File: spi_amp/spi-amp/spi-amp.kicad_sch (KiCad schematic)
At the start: 35 parts, among them J1 IN+, J2 IN-, J3 OUT+, J4 OUT-, J5 Conn_01x02, J7 Conn_01x06, U1 LMH6401, U2 LM78M05_TO220, U3 LTV-847S, U4 74LVC1G04, U5 74LVC1G04, U6 74LVC1G04

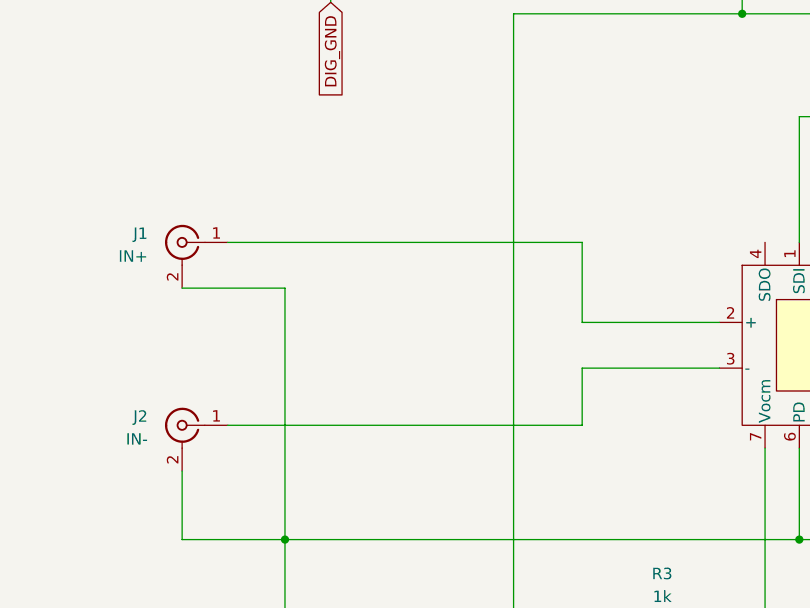
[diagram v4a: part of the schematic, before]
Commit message: Added input capacitors.
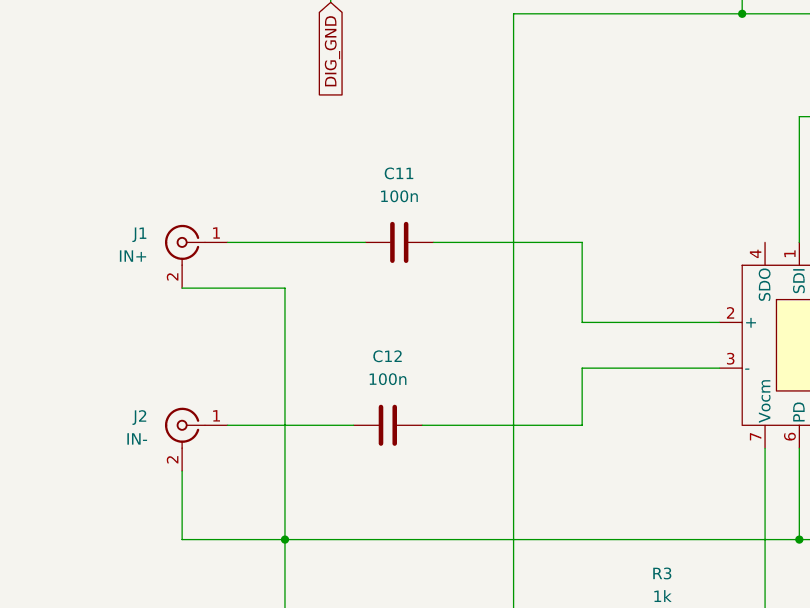
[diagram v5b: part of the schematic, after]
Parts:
- added C11, C12: 100n, Capacitor_SMD:C_0805_2012Metric_Pad1.18x1.45mm_HandSolder, symbol Device:C
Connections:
- net at J2.1 (In): now also C12.1; no longer U1.3 (-)
- net at J1.1 (In): now also C11.1; no longer U1.2 (+)
- new net: C11.2, U1.2 (+)
- new net: C12.2, U1.3 (-)
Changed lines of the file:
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@@
-	(wire
-		(pts
-			(xy 52.07 81.28) (xy 91.44 81.28)
-		)
-		(stroke
-			(width 0)
-			(type default)
-		)
-	)
 	(wire
 		(pts
@@
 	(wire
 		(pts
+			(xy 52.07 81.28) (xy 67.31 81.28)
+		)
+		(stroke
+			(width 0)
+			(type default)
+		)
+	)
+	(wire
+		(pts
 			(xy 119.38 81.28) (xy 119.38 71.12)
 		)
@@
 	(wire
 		(pts
+			(xy 73.66 101.6) (xy 91.44 101.6)
+		)
+		(stroke
+			(width 0)
+			(type default)
+		)
+	)
+	(wire
+		(pts
 			(xy 83.82 124.46) (xy 96.52 124.46)
 		)
@@
 	(wire
 		(pts
+			(xy 91.44 81.28) (xy 74.93 81.28)
+		)
+		(stroke
+			(width 0)
+			(type default)
+		)
+	)
+	(wire
+		(pts
 			(xy 224.79 34.29) (xy 224.79 142.24)
 		)
@@
 	(wire
 		(pts
-			(xy 52.07 101.6) (xy 91.44 101.6)
-		)
-		(stroke
-			(width 0)
-			(type default)
-		)
-	)
-	(wire
-		(pts
 			(xy 153.67 46.99) (xy 170.18 46.99)
 		)
@@
 		(pts
 			(xy 54.61 34.29) (xy 63.5 34.29)
+		)
+		(stroke
+			(width 0)
+			(type default)
+		)
+	)
+	(wire
+		(pts
+			(xy 52.07 101.6) (xy 66.04 101.6)
 		)
 		(stroke
@@
 	(symbol
 		(lib_id "Device:C")
+		(at 71.12 81.28 90)
+		(unit 1)
+		(body_style 1)
+		(exclude_from_sim no)
+		(in_bom yes)
+		(on_board yes)
+		(in_pos_files yes)
+		(dnp no)
+		(fields_autoplaced yes)
+		(property "Reference" "C11"
+			(at 71.12 73.66 90)
+			(show_name no)
+			(do_not_autoplace no)
+			(effects
+				(font
+					(size 1.27 1.27)
+				)
+			)
+		)
+		(property "Value" "100n"
+			(at 71.12 76.2 90)
+			(show_name no)
+			(do_not_autoplace no)
+			(effects
+				(font
+					(size 1.27 1.27)
+				)
+			)
+		)
+		(property "Footprint" "Capacitor_SMD:C_0805_2012Metric_Pad1.18x1.45mm_HandSolder"
+			(at 74.93 80.3148 0)
+			(hide yes)
+			(show_name no)
+			(do_not_autoplace no)
+			(effects
+				(font
+					(size 1.27 1.27)
+				)
+			)
+		)
+		(property "Datasheet" ""
+			(at 71.12 81.28 0)
+			(hide yes)
+			(show_name no)
+			(do_not_autoplace no)
+			(effects
+				(font
+					(size 1.27 1.27)
+				)
+			)
+		)
+		(property "Description" "Unpolarized capacitor"
+			(at 71.12 81.28 0)
+			(hide yes)
+			(show_name no)
+			(do_not_autoplace no)
+			(effects
+				(font
+					(size 1.27 1.27)
+				)
+			)
+		)
+		(pin "1"
+		)
+		(pin "2"
+		)
+		(instances
+			(project "spi-amp"
+				(path "/7b23121c-57e3-4266-95bd-22be68c11a42"
+					(reference "C11")
+					(unit 1)
+				)
+			)
+		)
+	)
+	(symbol
+		(lib_id "Device:C")
 		(at 252.73 151.13 180)
 		(unit 1)
@@
 					(unit 1)
 				)
+			)
+		)
+	)
+	(symbol
+		(lib_id "Device:C")
+		(at 69.85 101.6 90)
+		(unit 1)
+		(body_style 1)
+		(exclude_from_sim no)
+		(in_bom yes)
+		(on_board yes)
+		(in_pos_files yes)
+		(dnp no)
+		(fields_autoplaced yes)
+		(property "Reference" "C12"
+			(at 69.85 93.98 90)
+			(show_name no)
+			(do_not_autoplace no)
+			(effects
+				(font
+					(size 1.27 1.27)
+				)
+			)
+		)
+		(property "Value" "100n"
+			(at 69.85 96.52 90)
+			(show_name no)
+			(do_not_autoplace no)
+			(effects
+				(font
+					(size 1.27 1.27)
+				)
+			)
+		)
+		(property "Footprint" "Capacitor_SMD:C_0805_2012Metric_Pad1.18x1.45mm_HandSolder"
+			(at 73.66 100.6348 0)
+			(hide yes)
+			(show_name no)
+			(do_not_autoplace no)
+			(effects
+				(font
+					(size 1.27 1.27)
+				)
+			)
+		)
+		(property "Datasheet" ""
+			(at 69.85 101.6 0)
+			(hide yes)
+			(show_name no)
+			(do_not_autoplace no)
+			(effects
+				(font
+					(size 1.27 1.27)
+				)
+			)
+		)
+		(property "Description" "Unpolarized capacitor"
+			(at 69.85 101.6 0)
+			(hide yes)
+			(show_name no)
+			(do_not_autoplace no)
+			(effects
+				(font
+					(size 1.27 1.27)
+				)
+			)
+		)
+		(pin "1"
+		)
+		(pin "2"
+		)
+		(instances
+			(project "spi-amp"
+				(path "/7b23121c-57e3-4266-95bd-22be68c11a42"
+					(reference "C12")
+					(unit 1)
+				)

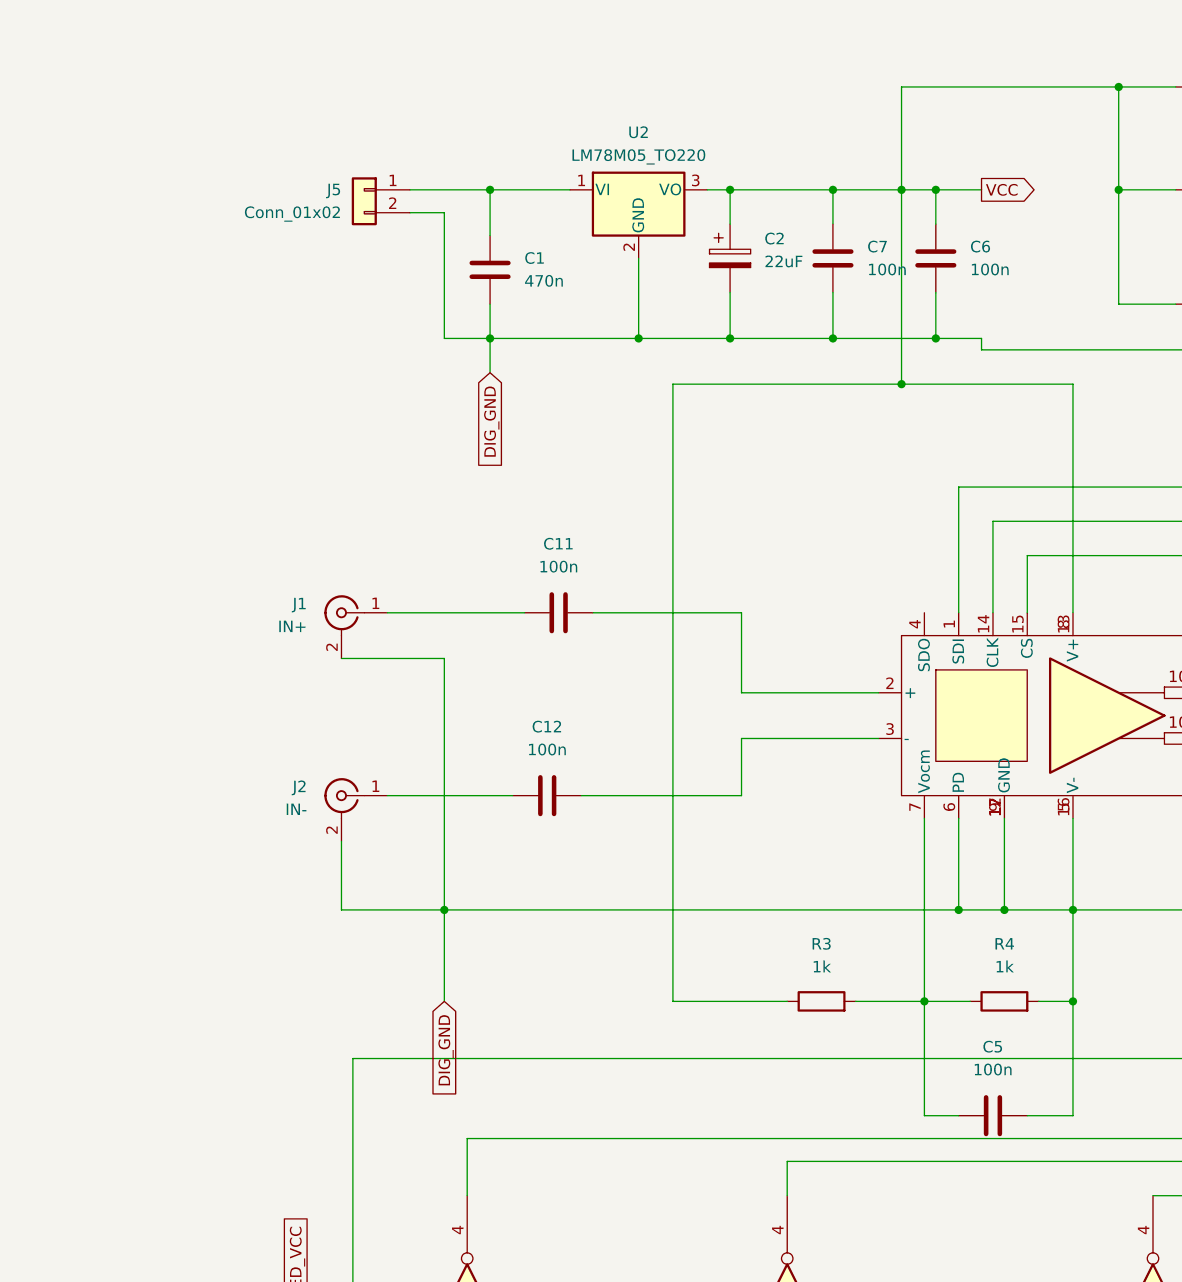
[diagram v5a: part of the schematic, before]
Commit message: Use 0402 for top layer RF components.
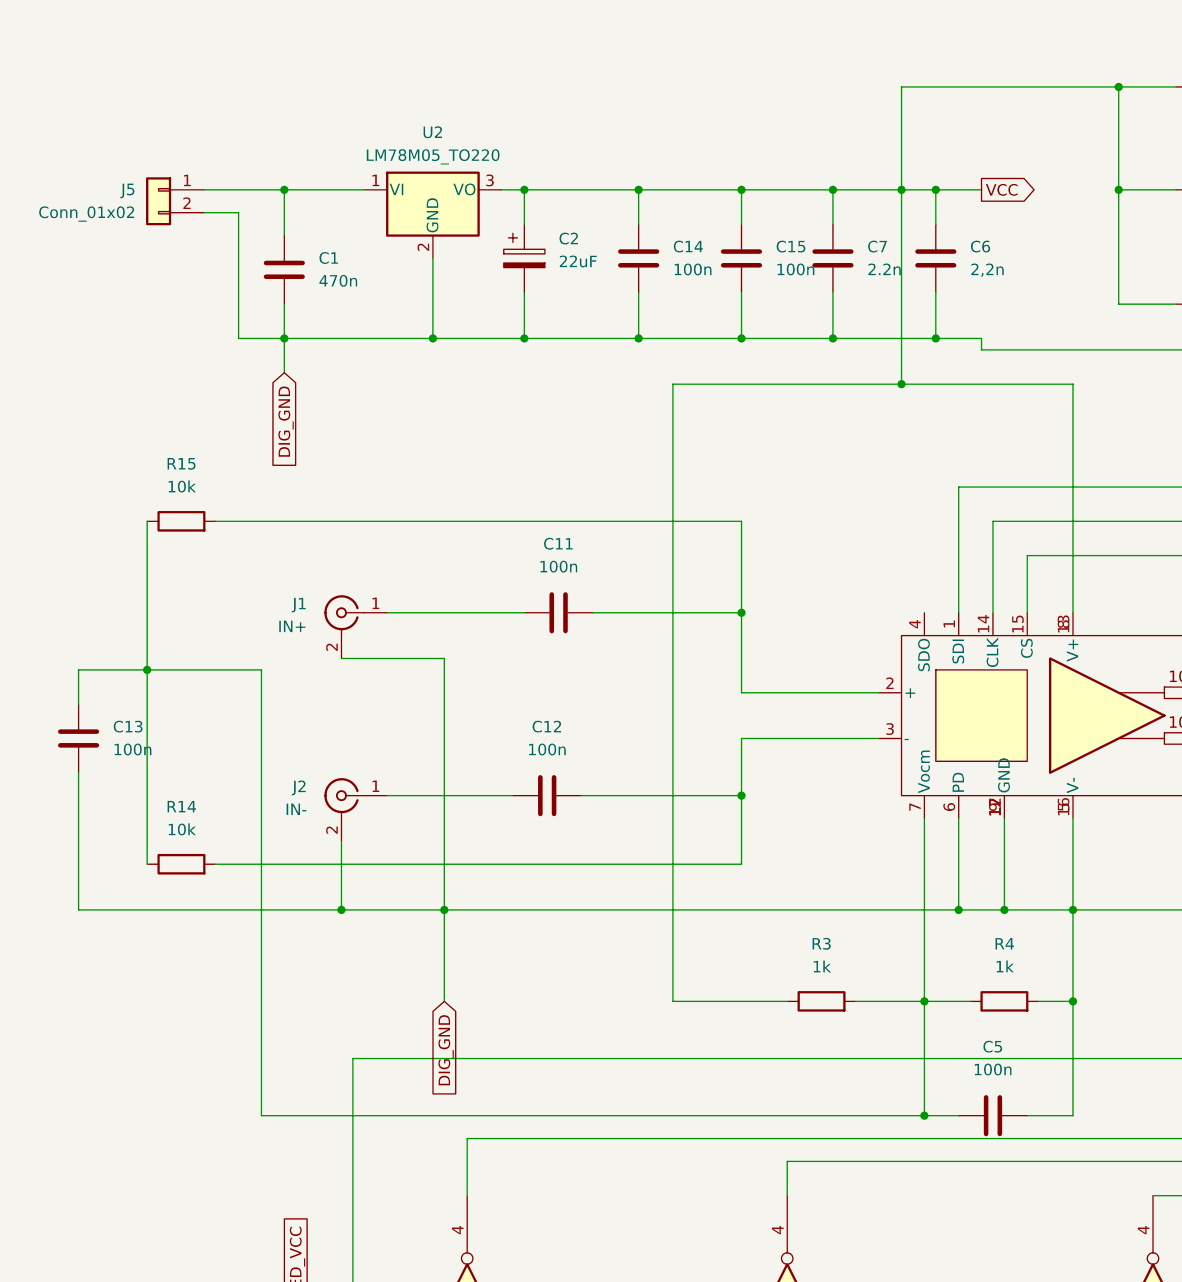
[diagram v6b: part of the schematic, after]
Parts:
- added C13, C14, C15: 100n, Capacitor_SMD:C_0805_2012Metric_Pad1.18x1.45mm_HandSolder, symbol Device:C
- added R14, R15: 10k, Resistor_SMD:R_0402_1005Metric_Pad0.72x0.64mm_HandSolder, symbol Device:R
- C11, C12, C3, C4: footprint Capacitor_SMD:C_0805_2012Metric_Pad1.18x1.45mm_HandSolder -> Capacitor_SMD:C_0402_1005Metric_Pad0.74x0.62mm_HandSolder
- C6: value 100n -> 2,2n; footprint Capacitor_SMD:C_0805_2012Metric_Pad1.18x1.45mm_HandSolder -> Capacitor_SMD:C_0402_1005Metric_Pad0.74x0.62mm_HandSolder
- C7: value 100n -> 2.2n; footprint Capacitor_SMD:C_0805_2012Metric_Pad1.18x1.45mm_HandSolder -> Capacitor_SMD:C_0402_1005Metric_Pad0.74x0.62mm_HandSolder
- R1, R2: footprint Resistor_SMD:R_0805_2012Metric_Pad1.20x1.40mm_HandSolder -> Resistor_SMD:R_0402_1005Metric_Pad0.72x0.64mm_HandSolder
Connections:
- net DIG_GND: now also C13.1, C14.1, C15.1
- net VCC: now also C14.2, C15.2
- net at C11.2, U1.2 (+): now also R15.2
- net at C5.1, R3.2, R4.1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: now also C13.2, R14.1, R15.1
- net at C12.2, U1.3 (-): now also R14.2
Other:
- moved on the sheet: C1, C2, J5, U2

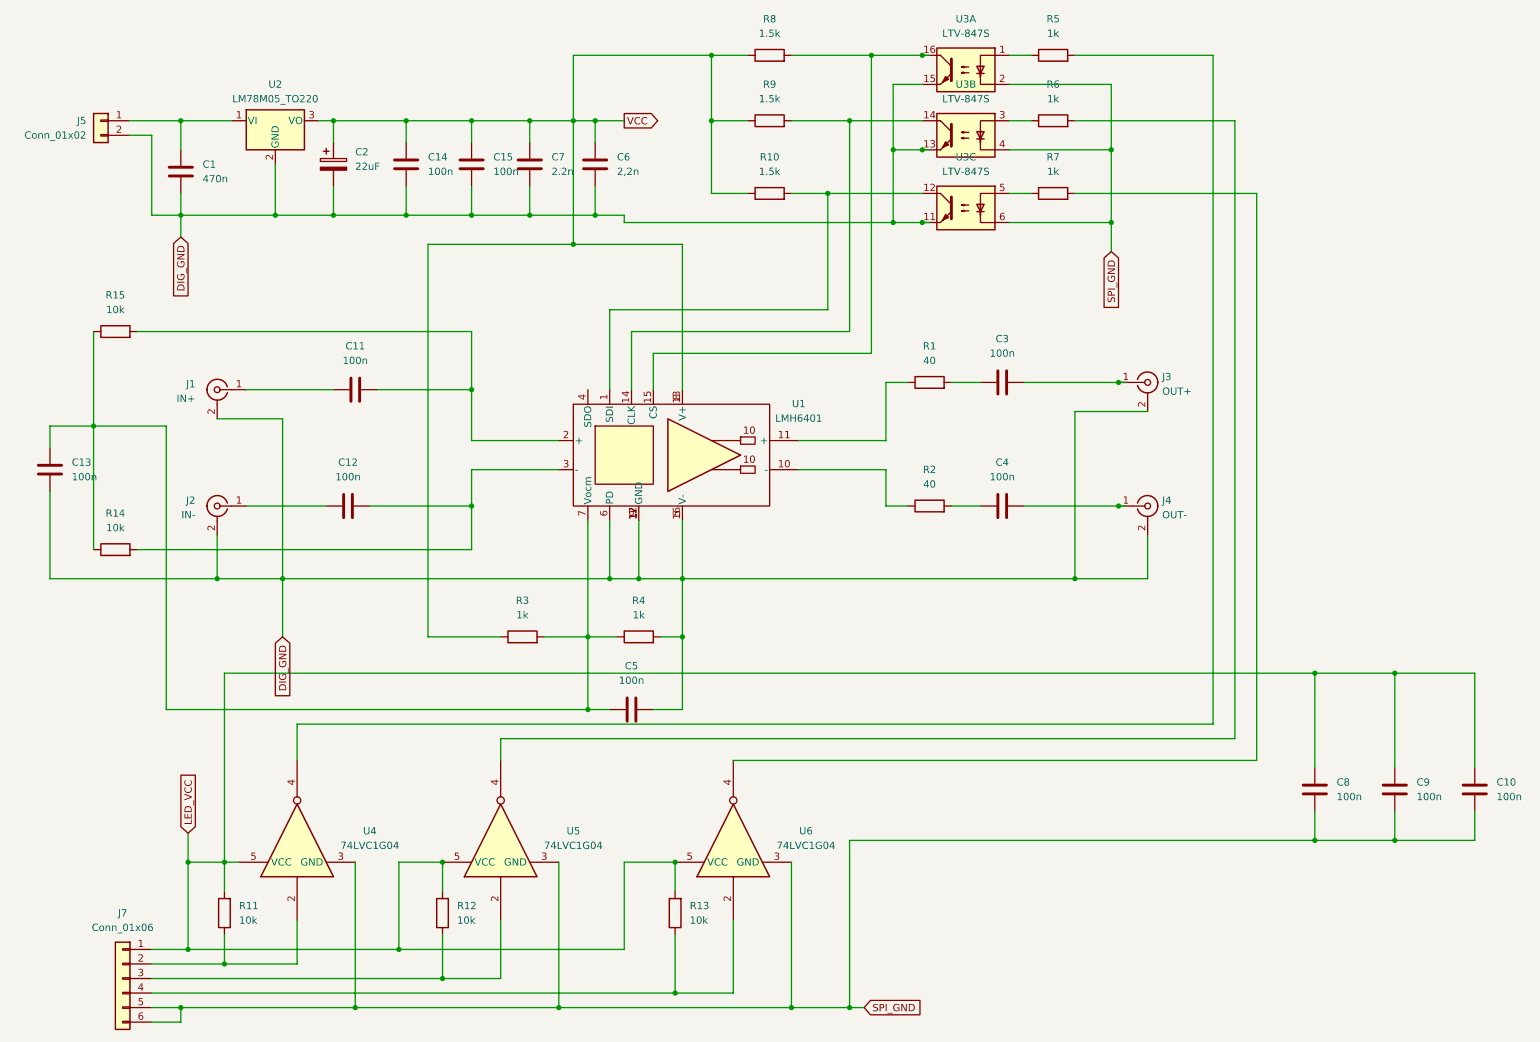
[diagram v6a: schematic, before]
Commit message: Changed to be compatible with EVM.
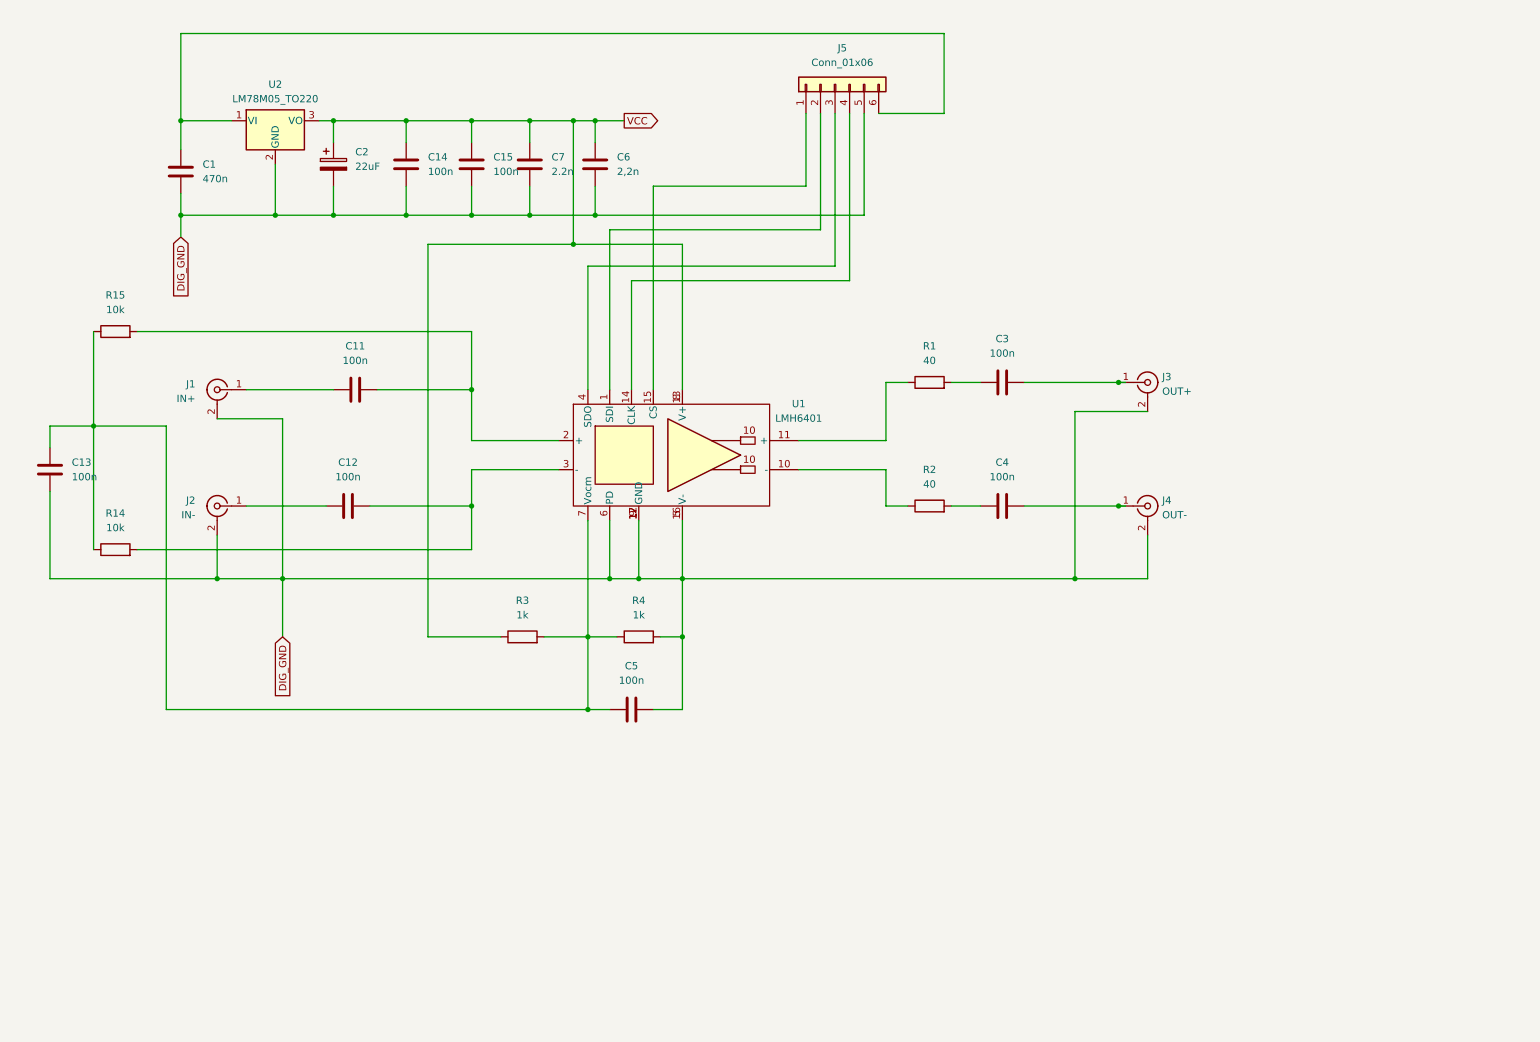
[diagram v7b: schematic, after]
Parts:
- removed C10, C8, C9: 100n, Capacitor_SMD:C_0805_2012Metric_Pad1.18x1.45mm_HandSolder, symbol Device:C
- removed J5: Conn_01x02, Connector_PinHeader_2.54mm:PinHeader_1x02_P2.54mm_Vertical, symbol Connector_Generic:Conn_01x02
- removed J7: Conn_01x06, Connector_PinHeader_2.54mm:PinHeader_1x06_P2.54mm_Vertical, symbol Connector_Generic:Conn_01x06
- removed R10, R8, R9: 1.5k, Resistor_SMD:R_0805_2012Metric_Pad1.20x1.40mm_HandSolder, symbol Device:R
- removed R11, R12, R13: 10k, Resistor_SMD:R_0805_2012Metric_Pad1.20x1.40mm_HandSolder, symbol Device:R
- removed R5, R6, R7: 1k, Resistor_SMD:R_0805_2012Metric_Pad1.20x1.40mm_HandSolder, symbol Device:R
- removed U3: LTV-847S, Package_DIP:SMDIP-16_W9.53mm, symbol Isolator:LTV-847S
- removed U4, U5, U6: 74LVC1G04, Package_TO_SOT_SMD:SOT-23-5_HandSoldering, symbol 74xGxx:74LVC1G04
- added J5: Conn_01x06, Connector_PinSocket_2.54mm:PinSocket_1x06_P2.54mm_Horizontal, symbol Connector_Generic:Conn_01x06
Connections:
- net DIG_GND: now also J5.5 (Pin_5)
- net at U1.14 (CLK): now also J5.4 (Pin_4)
- net at U1.15 (CS): now also J5.1 (Pin_1)
- net at C1.1, U2.1 (VI): now also J5.6 (Pin_6)
- net at U1.1 (SDI): now also J5.2 (Pin_2)
- net at U1.4 (SDO): now also J5.3 (Pin_3)
